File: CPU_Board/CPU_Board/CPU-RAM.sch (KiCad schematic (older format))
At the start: 2 parts

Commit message: SDRAM verdrahtet, STLINK conn, NRST, BOOT0, Oszillator. TODO: RS422, DCMI, SPI-Display, SD-Karte, Encoder, Step-Down
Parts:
- added C? (x22): 100n, Capacitor_SMD:C_0603_1608Metric, symbol Device:C_Small
- added C? (x2): 18p, Capacitor_SMD:C_0603_1608Metric, symbol Device:C_Small
- added C? (x4): 2.2u, Capacitor_SMD:C_1210_3225Metric, symbol Device:C_Small
- added FB?: 70R, Inductor_SMD:L_0603_1608Metric, symbol Device:Ferrite_Bead_Small
- added J?: Conn_01x06_Male, Connector_PinHeader_2.54mm:PinHeader_1x06_P2.54mm_Vertical, symbol Connector:Conn_01x06_Male
- added R? (x2): 10K, Resistor_SMD:R_0603_1608Metric, symbol Device:R_Small
- added R?: DNP, Resistor_SMD:R_0603_1608Metric, symbol Device:R_Small
- added Y?: 48MHz, symbol Device:Crystal_GND24
- U?: symbol PorjectLibrary:W9864G6KH -> CPU_Board-rescue:W9864G6KH-PorjectLibrary
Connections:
- net labels added: NRST, PF0, PF1, PF10, PF11, PF12, PF13, PF14, PF15, PF2, PF3, PF4, PF5, PF6, PF7, PF8, PF9, PG0, PG1, PG10, PG11, PG12, PG13, PG14, PG15, PG2, PG3, PG4, PG5, PG6, PG7, PG8, PG9, PH0, PH1, R_SWO, T_JTCK, T_JTMS, T_NRST, VREF
- wire segments 66 -> 237
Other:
- note added: "Decoupling caps"
- note added: "ST-LINK"
- note added: "TODO:\nSD-Karte \nStep-Down\nRS422\nDCMI\nEncoder\nSPI-Display"
- moved on the sheet: U?

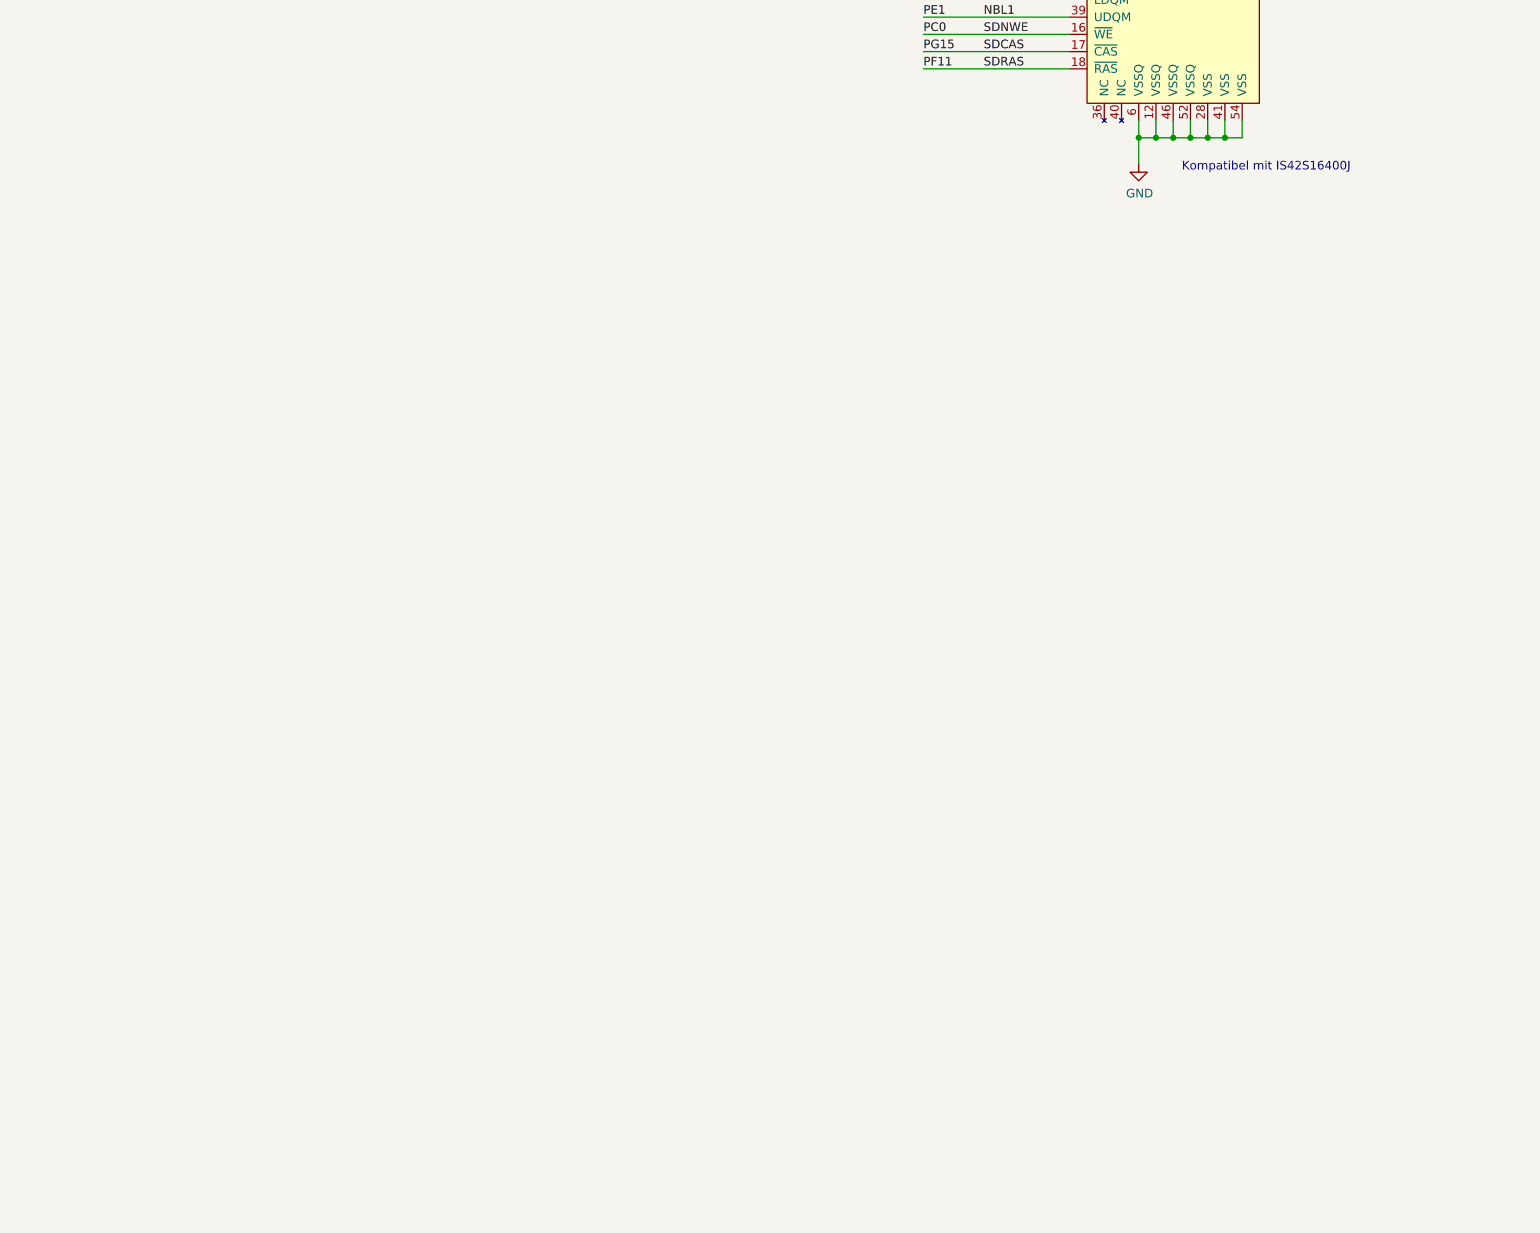
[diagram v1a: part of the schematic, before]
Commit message: rs485, sdcard, display connector, rotary encoder, camera connector; Step down and power
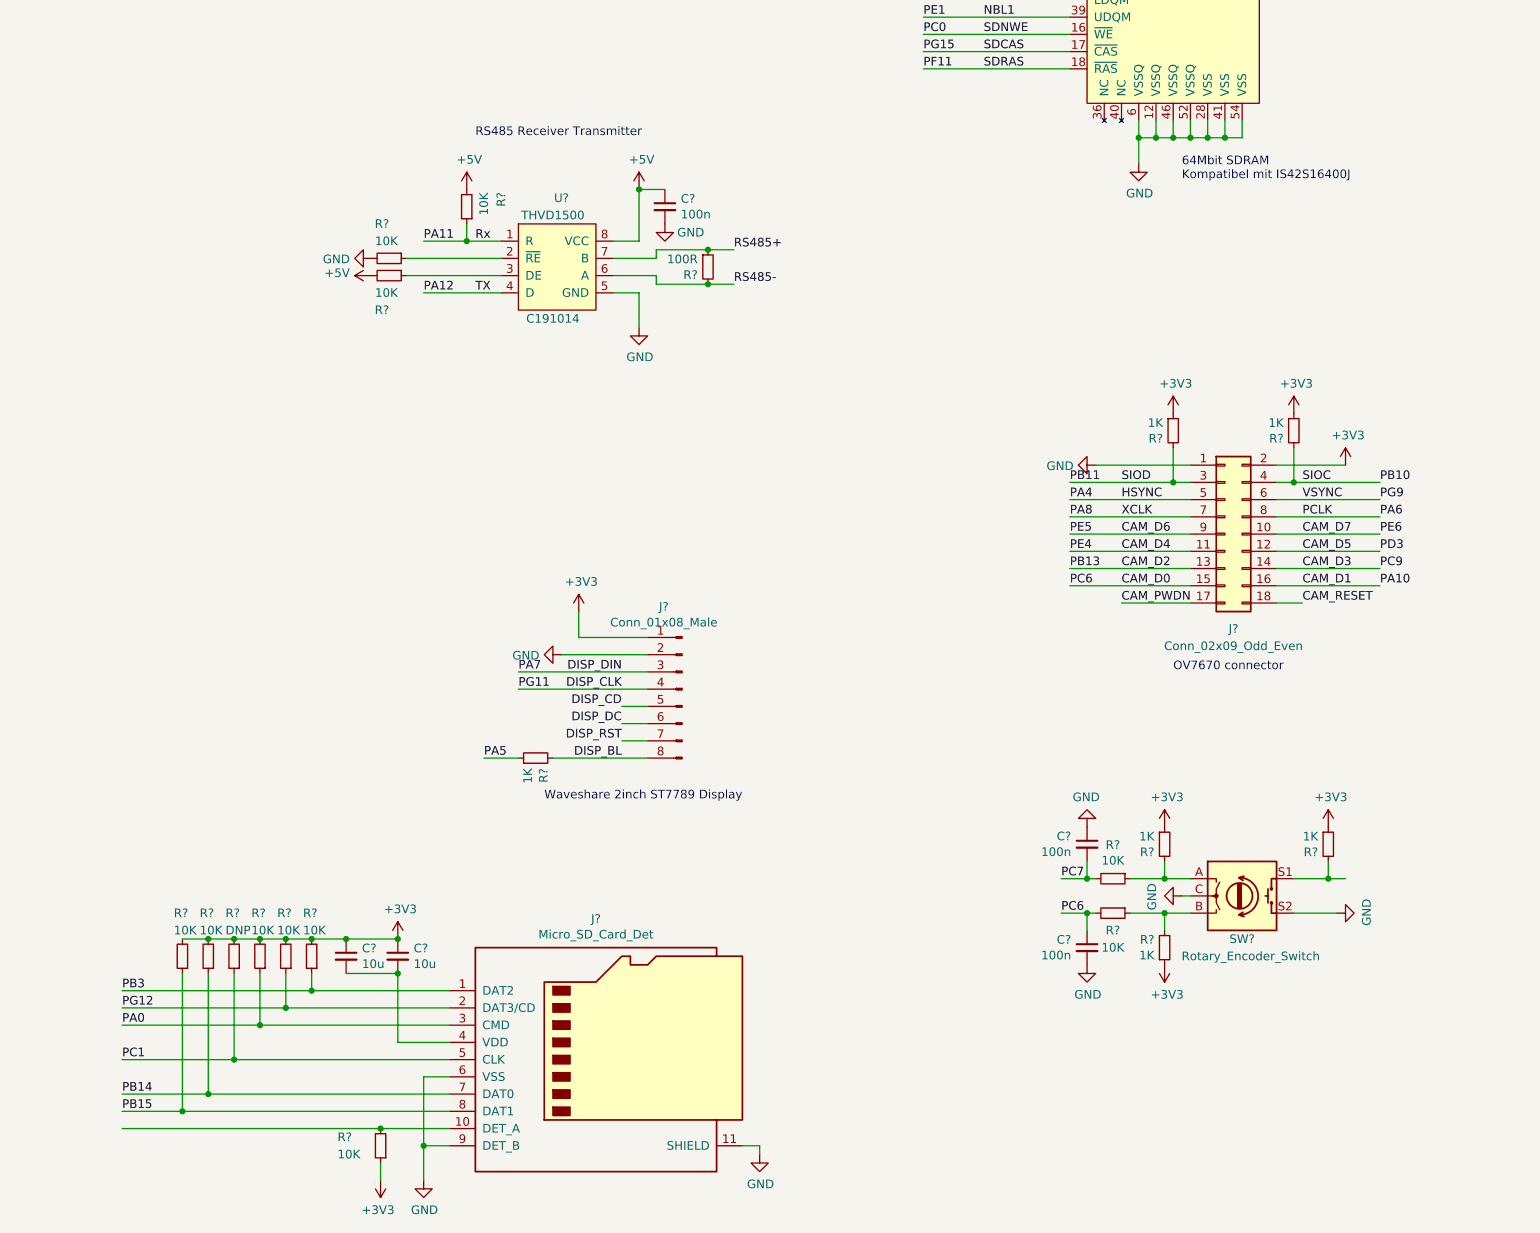
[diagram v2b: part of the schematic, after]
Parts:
- added C? (x3): 100n, Capacitor_SMD:C_0603_1608Metric, symbol Device:C_Small
- added C? (x2): 10u, Capacitor_SMD:C_0603_1608Metric, symbol Device:C_Small
- added J?: Conn_02x09_Odd_Even, symbol Connector_Generic:Conn_02x09_Odd_Even
- added J?: Conn_01x08_Male, symbol Connector:Conn_01x08_Male
- added J?: Micro_SD_Card_Det, symbol Connector:Micro_SD_Card_Det
- added R? (x6): 1K, Resistor_SMD:R_0603_1608Metric, symbol Device:R_Small
- added R? (x11): 10K, Resistor_SMD:R_0603_1608Metric, symbol Device:R_Small
- added R?: DNP, Resistor_SMD:R_0603_1608Metric, symbol Device:R_Small
- added R?: 100R, Resistor_SMD:R_0603_1608Metric, symbol Device:R_Small
- added SW?: Rotary_Encoder_Switch, symbol Device:Rotary_Encoder_Switch
- added U?: THVD1500, Package_SO:SOIC-8_3.9x4.9mm_P1.27mm, symbol PorjectLibrary:THVD1500
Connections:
- net +3V3: now also C?.1, C?.1, J?.1 (Pin_1), J?.2 (Pin_2), R?.1, R?.1, R?.1, R?.1, R?.1, R?.1, R?.2, R?.2, R?.2, R?.2, R?.2, R?.2
- net GND: now also C?.1, C?.2, C?.2, J?.1 (Pin_1), J?.11 (SHIELD), J?.2 (Pin_2), J?.6 (VSS), J?.9 (DET_B), R?.2, SW?.C, SW?.S2, U?.5 (GND)
- net PA0: now also J?.3 (CMD), R?.1
- net PA11: now also R?.1, U?.1 (R)
- net PA12: now also U?.4 (D)
- net PA5: now also R?.1
- net PA6: now also J?.8 (Pin_8)
- net PA8: now also J?.7 (Pin_7)
- net PB10: now also J?.4 (Pin_4), R?.2
- net PB11: now also J?.3 (Pin_3), R?.2
- net PB14: now also J?.7 (DAT0), R?.1
- net PB15: now also J?.8 (DAT1), R?.1
- net PB3: now also J?.1 (DAT2), R?.1
- net PC1: now also J?.5 (CLK), R?.1
- net PC7: now also C?.2, R?.2
- net PG12: now also J?.2 (DAT3/CD), R?.1
- net PG9: now also J?.6 (Pin_6)
- net PA10 renamed CAM_D1
- net CAM_D1: now also J?.16 (Pin_16)
- net PA4 renamed HSYNC
- net HSYNC: now also J?.5 (Pin_5)
- net PA7 renamed DISP_DIN
- net DISP_DIN: now also J?.3 (Pin_3)
- net PB13 renamed CAM_D2
- net CAM_D2: now also J?.13 (Pin_13)
- net PC6 renamed CAM_D0
- net CAM_D0: now also C?.1, J?.15 (Pin_15), R?.2
- net PC9 renamed CAM_D3
- net CAM_D3: now also J?.14 (Pin_14)
- net PD3 renamed CAM_D5
- net CAM_D5: now also J?.12 (Pin_12)
- net PE4 renamed CAM_D4
- net CAM_D4: now also J?.11 (Pin_11)
- net PE5 renamed CAM_D6
- net CAM_D6: now also J?.9 (Pin_9)
- net PE6 renamed CAM_D7
- net CAM_D7: now also J?.10 (Pin_10)
- net PG11 renamed DISP_CLK
- net DISP_CLK: now also J?.4 (Pin_4)
- new net: R?.1, R?.2, SW?.A
- new net: R?.1, R?.2, SW?.B
- new net: R?.2, SW?.S1
- new net: J?.10 (DET_A), R?.2
- new net: C?.2, C?.2, J?.4 (VDD)
- new net: R?.1, U?.2 (~RE)
- new net: R?.1, U?.3 (DE)
- new net +5V: C?.1, R?.2, R?.2, U?.8 (VCC)
- new net CAM_PWDN: J?.17 (Pin_17)
- new net CAM_RESET: J?.18 (Pin_18)
- new net DISP_BL: J?.8 (Pin_8), R?.2
- new net DISP_CD: J?.5 (Pin_5)
- new net DISP_DC: J?.6 (Pin_6)
- new net DISP_RST: J?.7 (Pin_7)
- new net RS485+: R?.1, U?.7 (B)
- new net RS485-: R?.2, U?.6 (A)
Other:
- note added: "64Mbit SDRAM\nKompatibel mit IS42S16400J"
- note added: "OV7670 connector"
- note added: "RS485 Receiver Transmitter"
- note added: "Waveshare 2inch ST7789 Display"
- note removed: "Kompatibel mit IS42S16400J"
